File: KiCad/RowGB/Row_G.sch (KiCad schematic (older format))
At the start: 37 parts, among them U701 RGB_WS2811, U702 RGB_WS2811, U703 RGB_WS2811, U704 RGB_WS2811, U705 RGB_WS2811, U706 RGB_WS2811, U707 RGB_WS2811, U708 RGB_WS2811, U709 RGB_WS2811, U710 RGB_WS2811, U711 RGB_WS2811, U712 RGB_WS2811, U713 RGB_WS2811, U714 RGB_WS2811, U715 RGB_WS2811, U716 RGB_WS2811

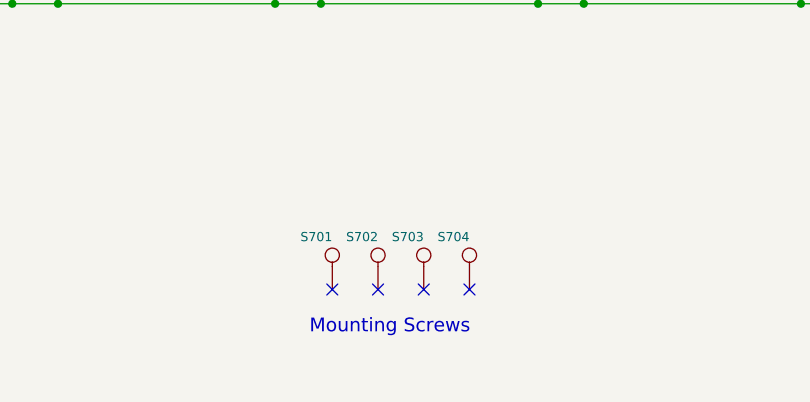
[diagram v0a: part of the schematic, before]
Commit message: TiM : Need to add legend for stacking connectors.
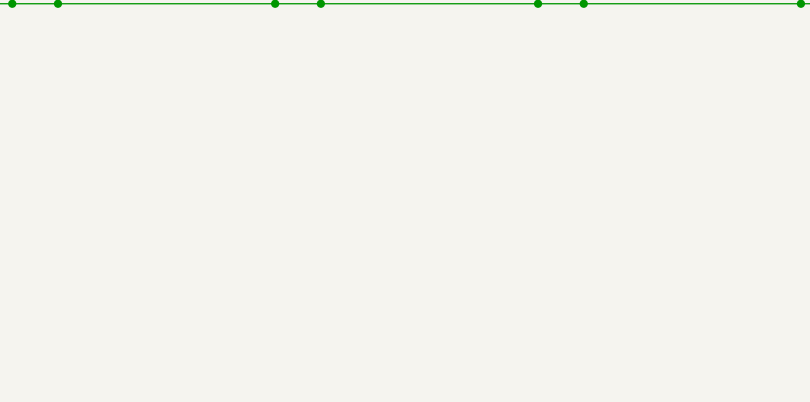
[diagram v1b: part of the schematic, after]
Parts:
- removed S701, S702, S703, S704: CONN_1, Screw, symbol CONN_1
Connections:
- no-connect marks 20 -> 16
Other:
- note removed: "Mounting Screws"
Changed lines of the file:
@@
-EESchema Schematic File Version 2  date Tuesday 12 February 2013 12:06:40 AM IST
+EESchema Schematic File Version 2  date 2/13/2013 1:59:50 PM
 LIBS:RowGB_sym
 LIBS:power
@@
 Sheet 3 9
 Title "TiM - The Intelligent Matrix"
-Date "11 feb 2013"
+Date "13 feb 2013"
 Rev ""
 Comp "WyoLum"
@@
 	1    0    0    -1
 $EndComp
-$Comp
-L CONN_1 S701
-U 1 1 5118AB7A
-P 5300 6650
-F 0 "S701" V 5380 6650 40  0000 L CNN
-F 1 "CONN_1" H 5300 6705 30  0001 C CNN
-F 2 "Screw" H 5300 6805 30  0001 C CNN
-	1    5300 6650
-	0    -1   -1   0
-$EndComp
-$Comp
-L CONN_1 S702
-U 1 1 5118AB74
-P 5500 6650
-F 0 "S702" V 5580 6650 40  0000 L CNN
-F 1 "CONN_1" H 5500 6705 30  0001 C CNN
-F 2 "Screw" H 5500 6805 30  0001 C CNN
-	1    5500 6650
-	0    -1   -1   0
-$EndComp
-$Comp
-L CONN_1 S703
-U 1 1 51189823
-P 5700 6650
-F 0 "S703" V 5780 6650 40  0000 L CNN
-F 1 "CONN_1" H 5700 6705 30  0001 C CNN
-F 2 "Screw" H 5700 6805 30  0001 C CNN
-	1    5700 6650
-	0    -1   -1   0
-$EndComp
-$Comp
-L CONN_1 S704
-U 1 1 5118AB64
-P 5900 6650
-F 0 "S704" V 5980 6650 40  0000 L CNN
-F 1 "CONN_1" H 5900 6705 30  0001 C CNN
-F 2 "Screw" H 5900 6805 30  0001 C CNN
-	1    5900 6650
-	0    -1   -1   0
-$EndComp
-NoConn ~ 5300 6800
-NoConn ~ 5500 6800
-NoConn ~ 5700 6800
-NoConn ~ 5900 6800
-Text Notes 5200 7000 0    60   ~ 0
-Mounting Screws
 Text Label 1250 6350 0    60   ~ 0
 5V
